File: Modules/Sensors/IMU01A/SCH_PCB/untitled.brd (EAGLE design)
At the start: 30 x 40.1 mm, 22 parts, among them X1 MMA8451Q, X2 A3G4250D, X3 SROUB3M, X4 SROUB3M, X5 SROUB3M, X6 SROUB3M

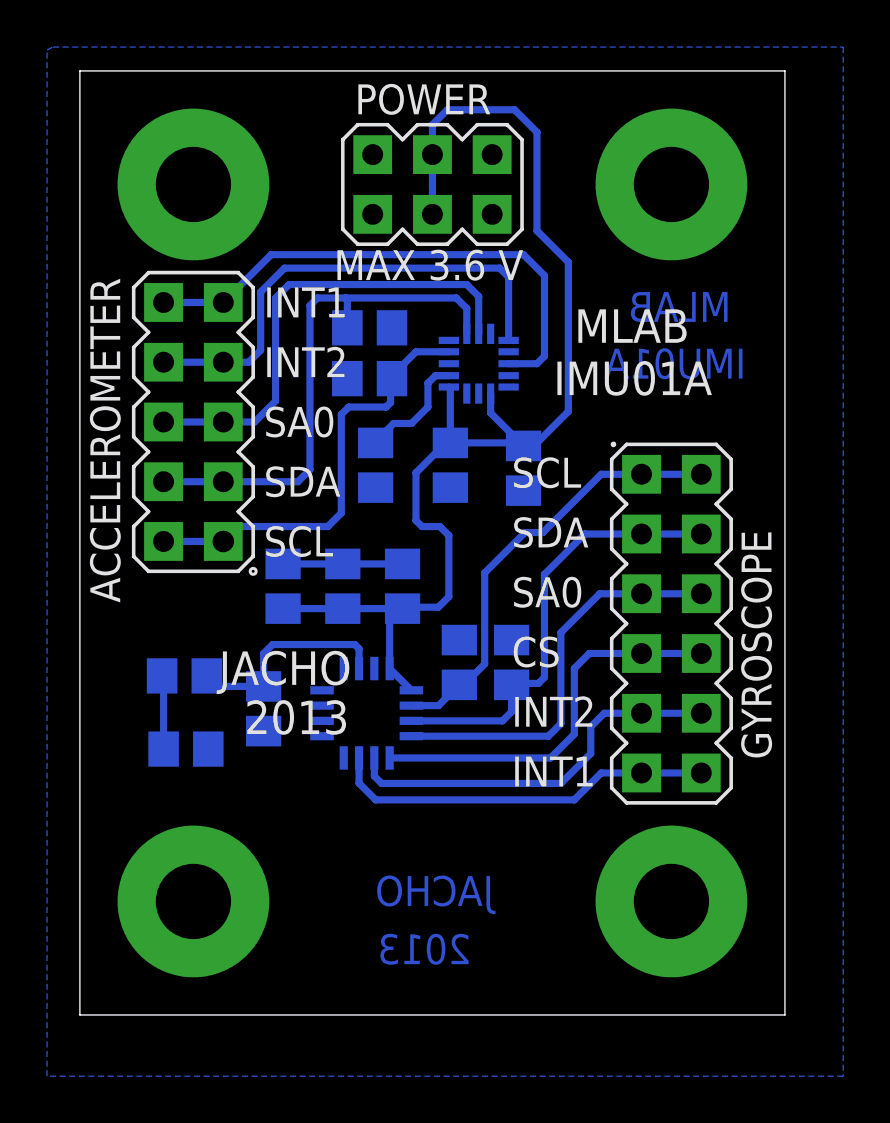
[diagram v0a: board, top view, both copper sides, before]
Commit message: 
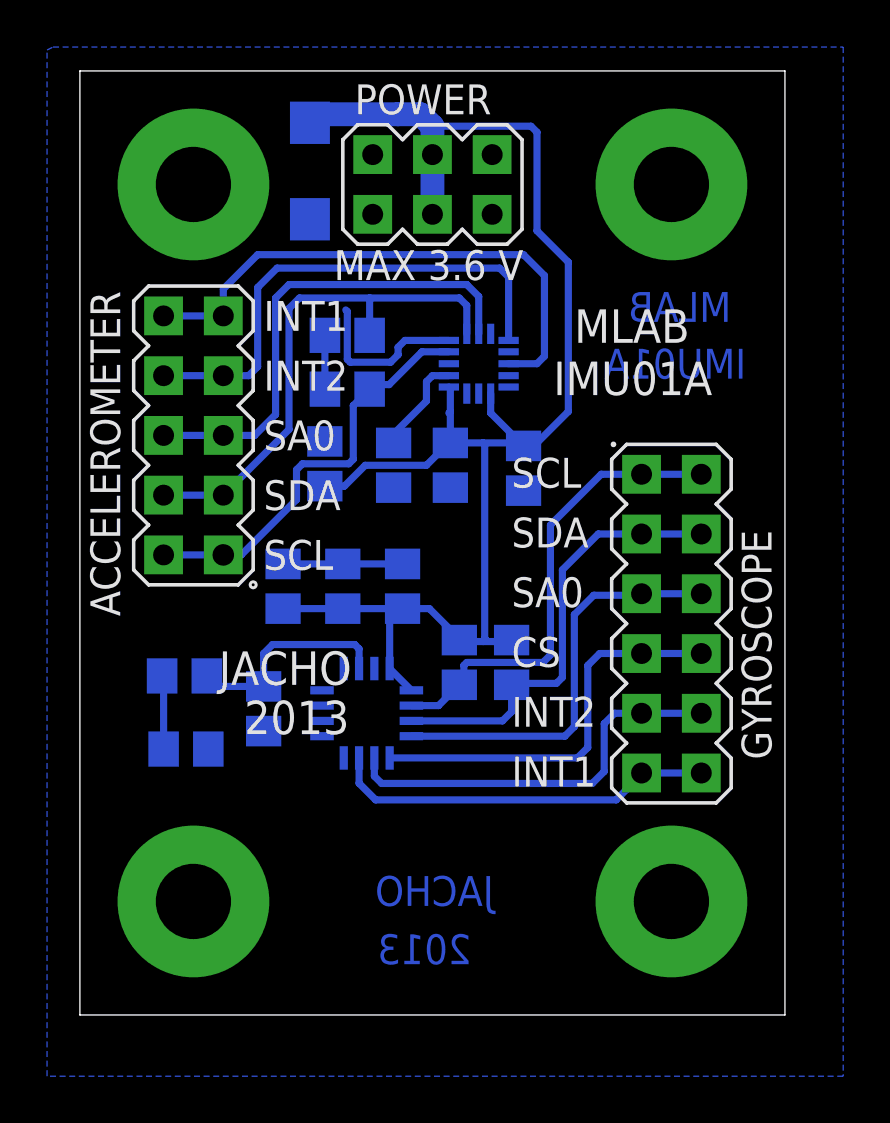
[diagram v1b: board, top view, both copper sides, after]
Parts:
- added D1: (no value), moje:SMA
- added R6: 0R, rcl:R0805
- moved R2 1.05 mm to (11.6, 26.9)
- moved R1 1.00 mm to (11.6, 29.1), turned to 180 degrees
- moved C3 0.76 mm to (13.6, 23.6)
- moved SV3 0.57 mm to (5.08, 24.9)
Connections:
- new net N$7: R1.1, R2.1, R6.2
- net +VCC: now also D1.K, R4.1, R5.1, R6.1
- net GND: now also D1.A; no longer R1.1, R2.1, R4.1, R5.1
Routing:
- net +VCC: track 52.6 -> 68.0 mm
- net GND: track 5.08 -> 12.1 mm
- net N$7: track 0.00 -> 2.37 mm
- net N$14: track 18.7 -> 20.1 mm
- net N$5: track 5.20 -> 4.28 mm
- net N$2: track 18.7 -> 17.8 mm
- net N$12: track 22.5 -> 23.4 mm
- net N$13: track 20.6 -> 21.4 mm
- net N$11: track 16.5 -> 17.2 mm
- net N$3: track 20.2 -> 20.8 mm
- net N$6: track 17.1 -> 17.6 mm

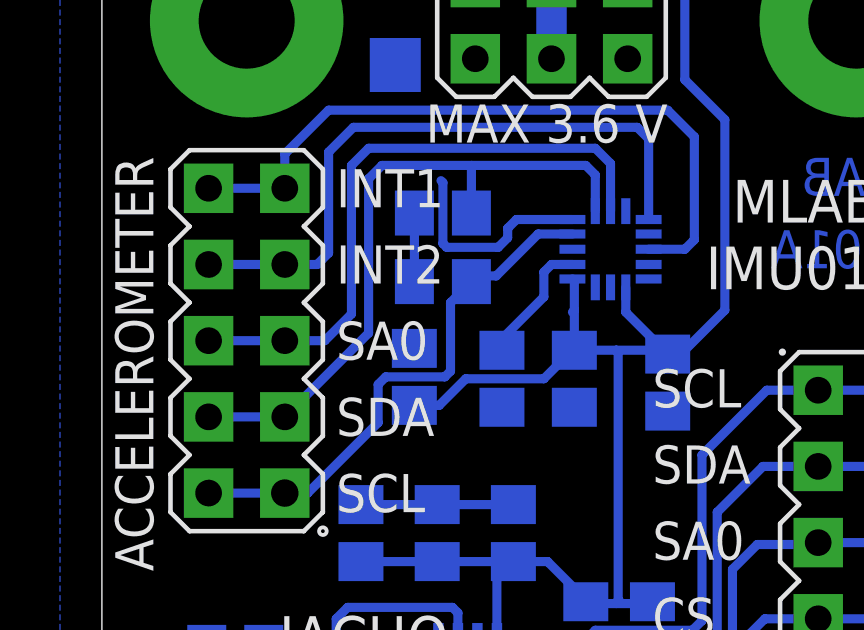
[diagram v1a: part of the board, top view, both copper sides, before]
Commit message: 
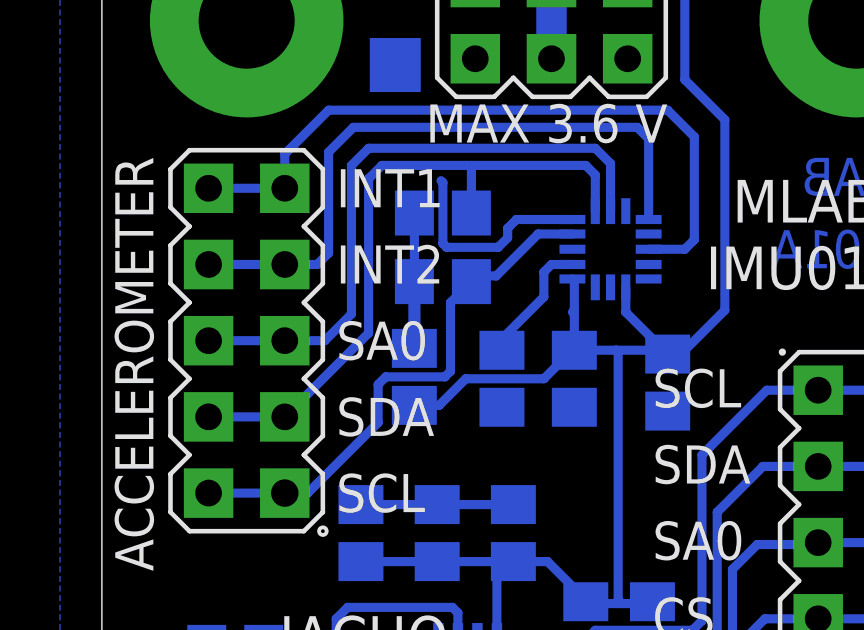
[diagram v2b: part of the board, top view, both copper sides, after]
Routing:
- net N$7: track 2.37 -> 4.60 mm
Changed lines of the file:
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@@
 <wire x1="10.6705" y1="26.863" x2="10.668" y2="26.8605" width="0.3048" layer="16"/>
 <wire x1="10.6705" y1="26.863" x2="10.7315" y2="26.924" width="0.3048" layer="16"/>
-<wire x1="10.6705" y1="26.863" x2="10.6705" y2="26.8605" width="0" layer="19" extent="16-16"/>
-<wire x1="10.668" y1="24.6355" x2="10.6705" y2="26.8605" width="0" layer="19" extent="16-16"/>
+<wire x1="10.668" y1="24.6355" x2="10.6705" y2="24.6355" width="0.4064" layer="16"/>
+<wire x1="10.6705" y1="24.6355" x2="10.6705" y2="26.8605" width="0.4064" layer="16"/>
+<wire x1="10.6705" y1="26.8605" x2="10.6705" y2="26.863" width="0" layer="19" extent="16-16"/>
 </signal>
 </signals>

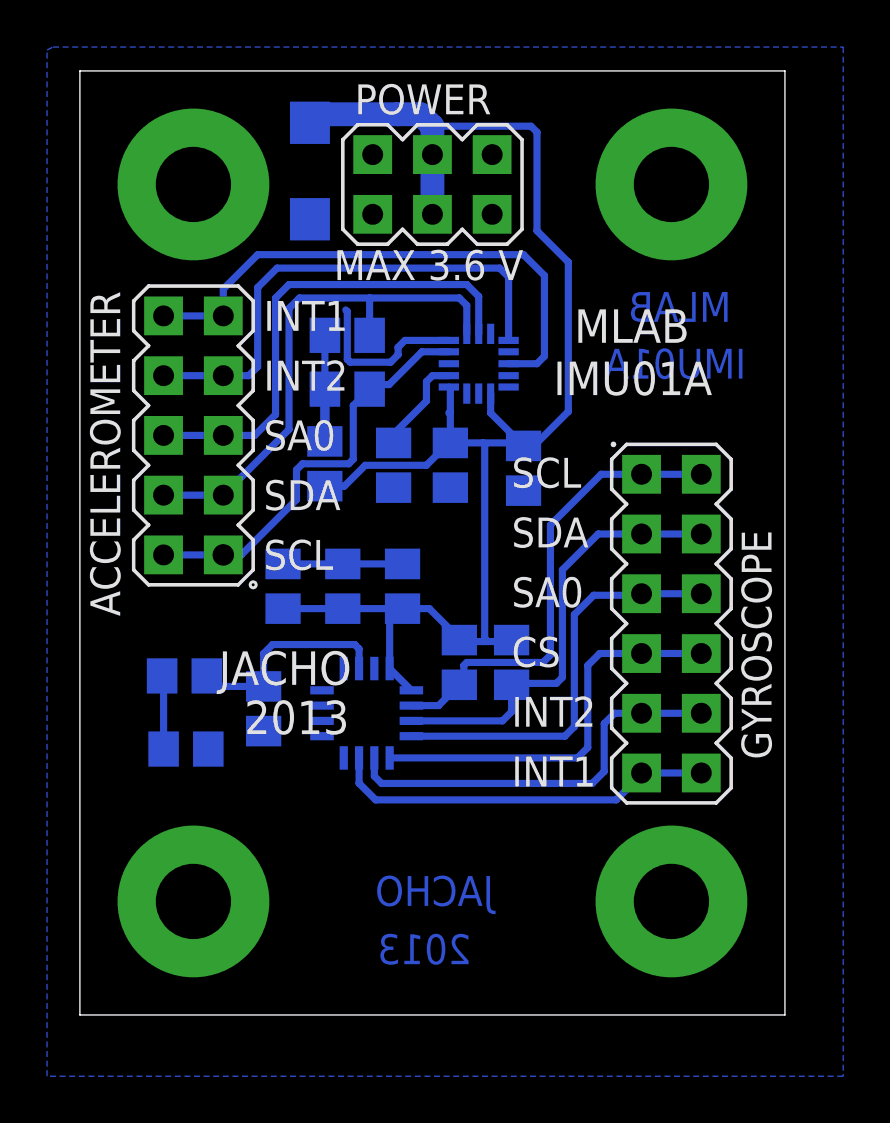
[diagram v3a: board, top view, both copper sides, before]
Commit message: 
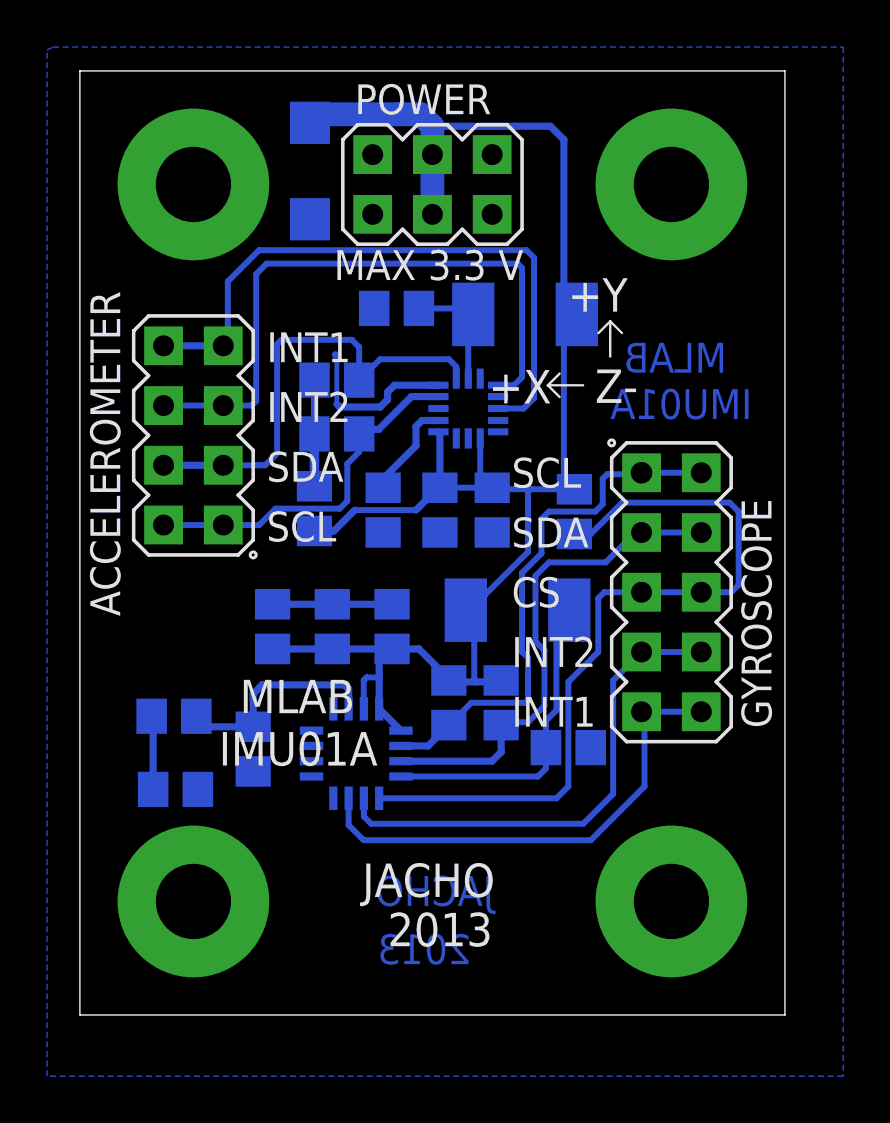
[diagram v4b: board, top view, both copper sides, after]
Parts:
- removed SV3: (no value), moje_hrebinky:MA05-2
- added R10, R8: 0R, moje_R:0805
- added R11, R9: (no value), rcl:R2010
- added R7: 10k, rcl:R0805
- added SV4: (no value), moje_hrebinky:MA04-2
- SV2: device moje_hrebinky:MA06-2 -> moje_hrebinky:MA05-2
- moved C1 2.22 mm to (17.8, 21.7)
- moved X1 1.96 mm to (16.8, 26.0)
- moved C2 1.96 mm to (15.6, 21.7)
- moved C3 1.96 mm to (13.1, 21.7)
- moved R1 1.96 mm to (11.2, 27.2)
- moved R6 1.96 mm to (10.2, 21.8)
- moved R2 1.96 mm to (11.2, 25.0)
- moved C4 1.77 mm to (13.5, 16.8)
- moved C6 1.77 mm to (8.45, 16.8)
- moved C5 1.77 mm to (11.0, 16.8)
- moved R3 1.77 mm to (4.32, 9.84)
- moved R4 1.77 mm to (15.9, 13.5)
- moved R5 1.77 mm to (18.2, 13.5)
- moved C8 1.77 mm to (7.62, 11.6)
- moved C9 1.77 mm to (4.25, 13.0)
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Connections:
- removed net N$3: SV3.5, SV3.6, X1.7
- removed net N$6: SV2.5, SV2.6, X2.4
- new net N$8: SV4.5, SV4.6, X1.9
- new net SA0: R10.1, R11.2, X2.4
- net +VCC: now also R11.1, R7.1, R9.1, X2.15
- net GND: now also R10.2, R8.2, X3.P$1, X4.P$1, X5.P$1, X6.P$1; no longer X1.3, X2.15
- net N$1: now also SV4.3, SV4.4; no longer SV3.3, SV3.4
- net N$10: now also SV2.10, SV2.9; no longer SV2.11, SV2.12
- net N$11: now also SV2.7, SV2.8; no longer SV2.10, SV2.9
- net N$12: now also SV4.7, SV4.8; no longer SV3.10, SV3.9
- net N$13: now also R8.1, R9.2, X1.7; no longer SV3.7, SV3.8, X1.9
- net N$2: now also SV4.1, SV4.2; no longer SV3.1, SV3.2
- net N$9: now also R7.2, SV2.5, SV2.6; no longer SV2.7, SV2.8
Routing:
- net N$8: track 0.00 -> 26.8 mm
- net N$3: track 20.8 -> 0.00 mm
- net N$6: track 17.6 -> 0.00 mm
- net N$9: track 17.1 -> 33.8 mm
- net N$13: track 21.4 -> 5.29 mm
- net SA0: track 0.00 -> 13.4 mm
- net +VCC: track 68.0 -> 76.5 mm
- net N$10: track 16.5 -> 20.7 mm
- net N$11: track 17.2 -> 21.1 mm
- net N$12: track 23.4 -> 26.7 mm
- net N$16: track 19.0 -> 21.7 mm
- net N$14: track 20.1 -> 22.8 mm
- net N$2: track 17.8 -> 15.3 mm
- net N$1: track 22.3 -> 19.9 mm
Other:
- board text added: "+X"
- board text added: "+Y"
- board text added: "MAX 3.3 V"
- board text added: "Z-"
- board text removed: "MAX 3.6 V"
- board text removed: "SA0"

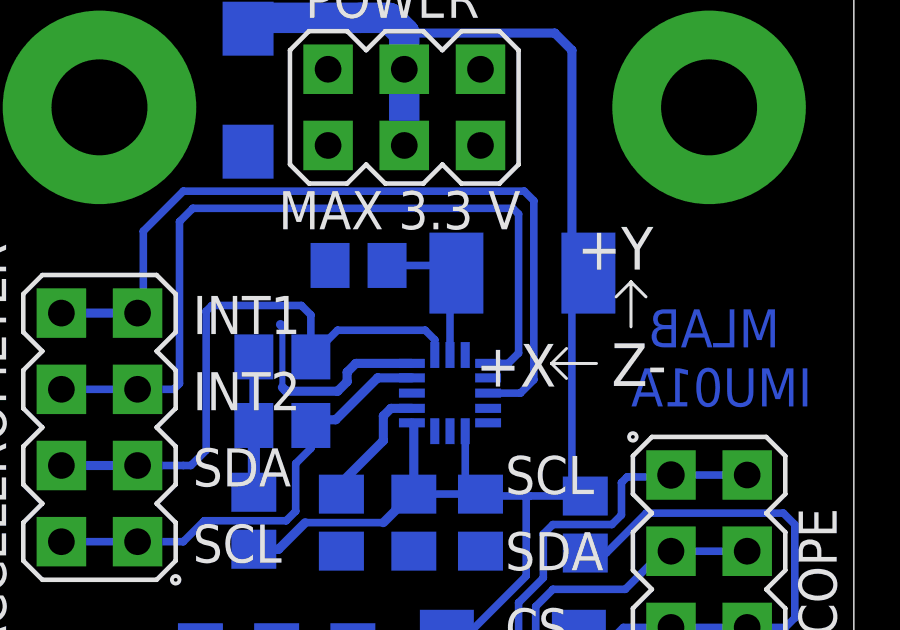
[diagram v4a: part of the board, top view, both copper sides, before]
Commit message: 
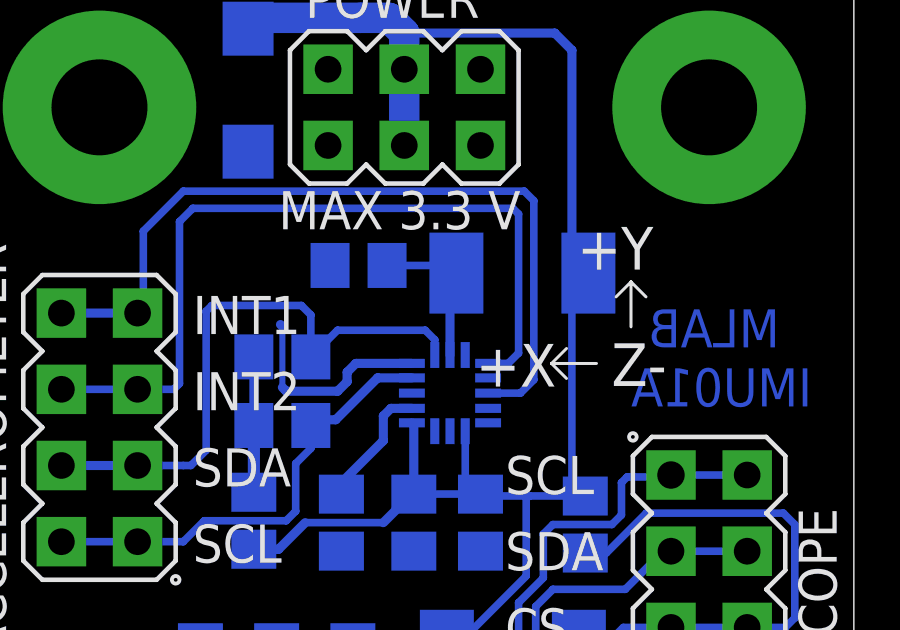
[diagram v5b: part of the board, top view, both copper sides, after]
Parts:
- D1: value (none) -> M4
